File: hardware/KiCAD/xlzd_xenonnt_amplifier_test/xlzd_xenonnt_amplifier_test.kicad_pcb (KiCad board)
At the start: 4 copper layers, 34 x 60 mm, 25 parts, among them J1 Conn_Coaxial, J2 Conn_Coaxial, J3 Conn_Coaxial, J4 Screw_Terminal_01x03, U1 OPA847xDBV, U3 OPA692xDBV

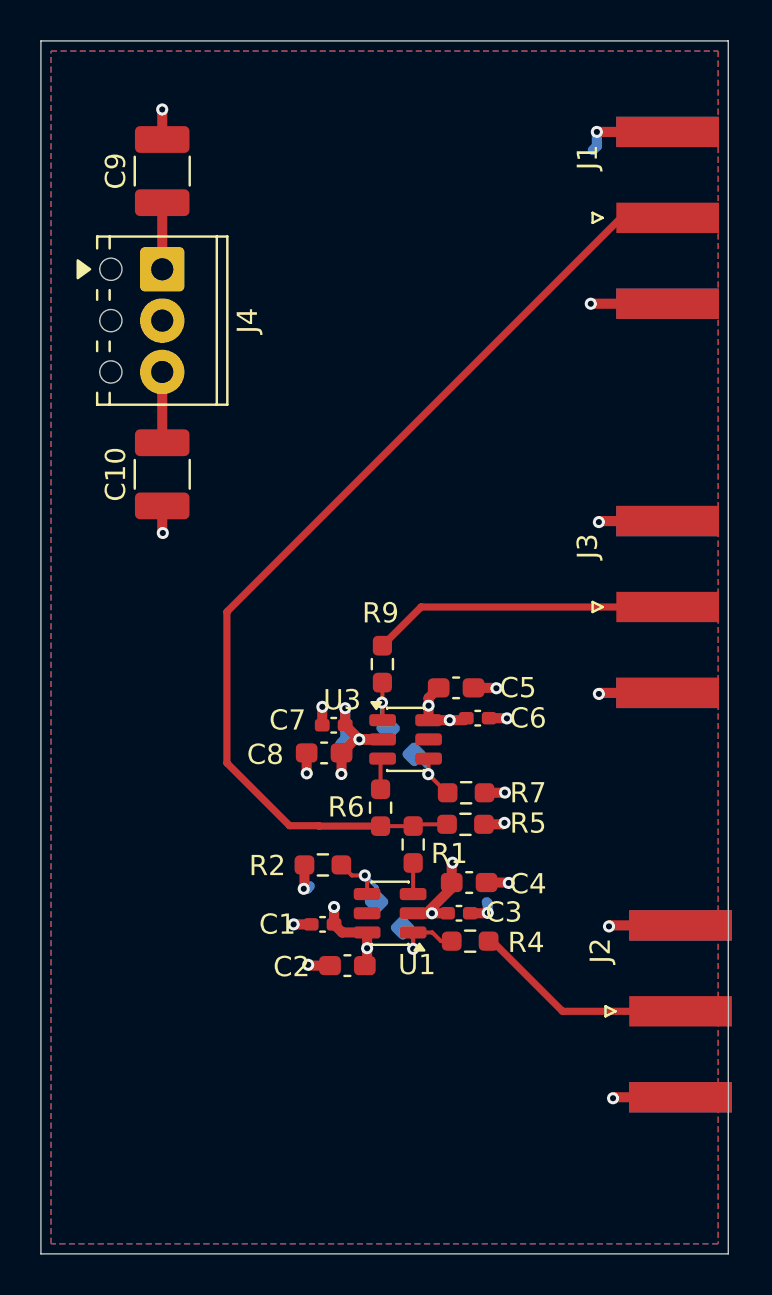
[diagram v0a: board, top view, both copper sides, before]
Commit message: Generated manufacturing artwork
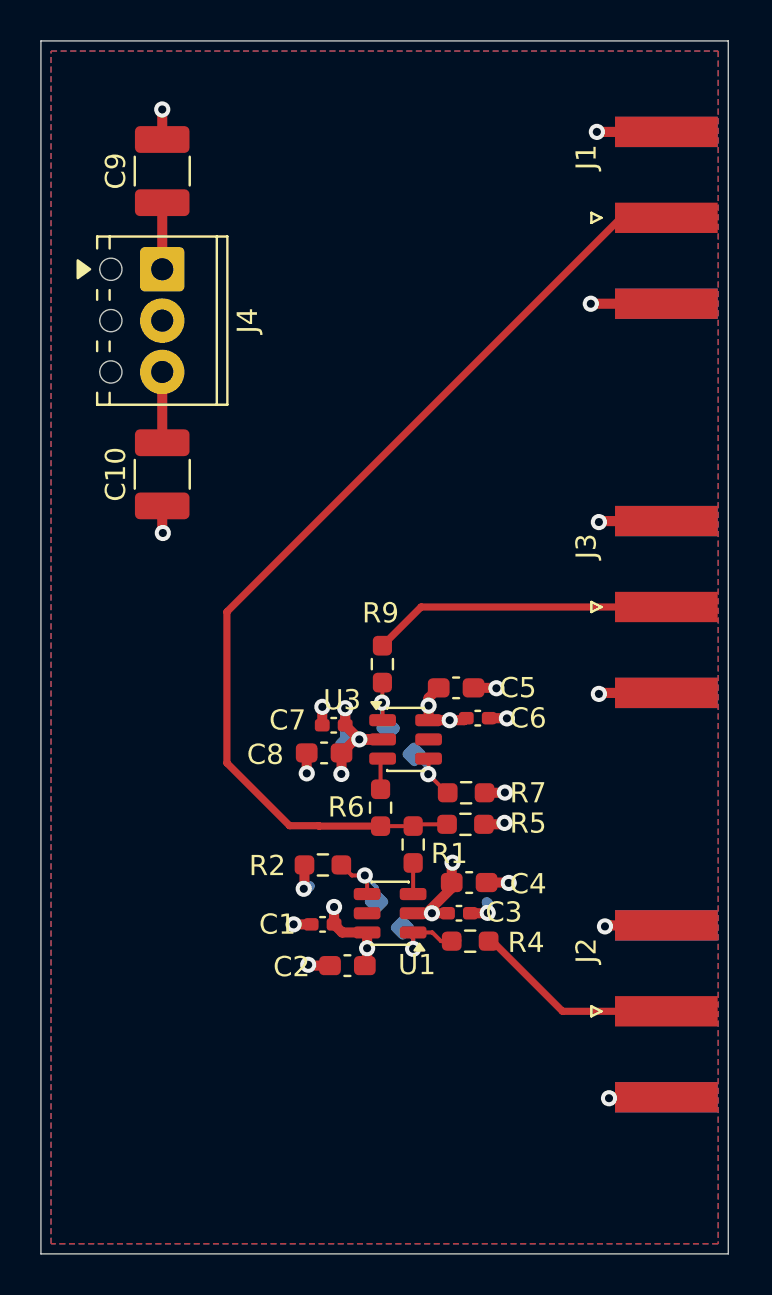
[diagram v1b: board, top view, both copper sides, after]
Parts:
- moved J2 0.70 mm to (75.9, 110.0)
- moved J1 0.06 mm to (75.9, 70.8)
- moved J3 0.06 mm to (75.9, 90.0)
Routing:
- net GND: track 36.9 -> 35.9 mm
- net /vout_high_g: track 10.9 -> 10.3 mm
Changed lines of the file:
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@@
 		(capping no)
 		(filling no)
-		(zone_defaults)
 		(pcbplotparams
 			(layerselection 0x00000000_00000000_55555555_5755f5ff)
@@
 	(footprint "Connector_Coaxial:SMA_Amphenol_132289_EdgeMount"
 		(layer "F.Cu")
-		(at 76 70.75)
+		(at 75.9375 70.75)
 		(descr "https://www.amphenolrf.com/library/download/link/link_id/595984/parent/132289/")
 		(tags "SMA")
@@
 	(footprint "Connector_Coaxial:SMA_Amphenol_132289_EdgeMount"
 		(layer "F.Cu")
-		(at 76 90)
+		(at 75.9375 90)
 		(descr "https://www.amphenolrf.com/library/download/link/link_id/595984/parent/132289/")
 		(tags "SMA")
@@
 	(footprint "Connector_Coaxial:SMA_Amphenol_132289_EdgeMount"
 		(layer "F.Cu")
-		(at 76.6375 110)
+		(at 75.9375 110)
 		(descr "https://www.amphenolrf.com/library/download/link/link_id/595984/parent/132289/")
 		(tags "SMA")
@@
 	(via
 		(at 68.05 95.51)
-		(size 0.6)
-		(drill 0.3)
+		(size 0.8)
+		(drill 0.4)
 		(layers "F.Cu" "B.Cu")
 		(net "GND")
@@
 	(via
 		(at 51 65.39)
-		(size 0.6)
-		(drill 0.3)
+		(size 0.8)
+		(drill 0.4)
 		(layers "F.Cu" "B.Cu")
 		(net "GND")
 	)
 	(via
-		(at 73.1 105.8)
-		(size 0.6)
-		(drill 0.3)
+		(at 72.9 105.8)
+		(size 0.8)
+		(drill 0.4)
 		(layers "F.Cu" "B.Cu")
 		(net "GND")
@@
 	(via
 		(at 58 103.94)
-		(size 0.6)
-		(drill 0.3)
+		(size 0.8)
+		(drill 0.4)
 		(layers "F.Cu" "B.Cu")
 		(net "GND")
@@
 	(via
 		(at 72.6 85.8)
-		(size 0.6)
-		(drill 0.3)
+		(size 0.8)
+		(drill 0.4)
 		(layers "F.Cu" "B.Cu")
 		(net "GND")
@@
 	(via
 		(at 72.2 75)
-		(size 0.6)
-		(drill 0.3)
+		(size 0.8)
+		(drill 0.4)
 		(layers "F.Cu" "B.Cu")
 		(net "GND")
@@
 	(via
 		(at 58.15 98.23)
-		(size 0.6)
-		(drill 0.3)
+		(size 0.8)
+		(drill 0.4)
 		(layers "F.Cu" "B.Cu")
 		(net "GND")
@@
 	(via
 		(at 67.93 100.68)
-		(size 0.6)
-		(drill 0.3)
+		(size 0.8)
+		(drill 0.4)
 		(layers "F.Cu" "B.Cu")
 		(net "GND")
@@
 	(via
 		(at 51.03 86.34)
-		(size 0.6)
-		(drill 0.3)
+		(size 0.8)
+		(drill 0.4)
 		(layers "F.Cu" "B.Cu")
 		(net "GND")
 	)
 	(via
-		(at 73.3 114.3)
-		(size 0.6)
-		(drill 0.3)
+		(at 73.1 114.3)
+		(size 0.8)
+		(drill 0.4)
 		(layers "F.Cu" "B.Cu")
 		(net "GND")
@@
 	(via
 		(at 58.92 94.94)
-		(size 0.6)
-		(drill 0.3)
+		(size 0.8)
+		(drill 0.4)
 		(layers "F.Cu" "B.Cu")
 		(net "GND")
@@
 	(via
 		(at 72.5 66.5)
-		(size 0.6)
-		(drill 0.3)
+		(size 0.8)
+		(drill 0.4)
 		(layers "F.Cu" "B.Cu")
 		(net "GND")
@@
 	(via
 		(at 67.53 94.02)
-		(size 0.6)
-		(drill 0.3)
+		(size 0.8)
+		(drill 0.4)
 		(layers "F.Cu" "B.Cu")
 		(net "GND")
@@
 	(via
 		(at 67.95 99.18)
-		(size 0.6)
-		(drill 0.3)
+		(size 0.8)
+		(drill 0.4)
 		(layers "F.Cu" "B.Cu")
 		(net "GND")
@@
 	(via
 		(at 58.22 107.7)
-		(size 0.6)
-		(drill 0.3)
+		(size 0.8)
+		(drill 0.4)
 		(layers "F.Cu" "B.Cu")
 		(net "GND")
@@
 	(via
 		(at 67.1 105.13)
-		(size 0.6)
-		(drill 0.3)
+		(size 0.8)
+		(drill 0.4)
 		(layers "F.Cu" "B.Cu")
 		(net "GND")
@@
 	(via
 		(at 68.14 103.65)
-		(size 0.6)
-		(drill 0.3)
+		(size 0.8)
+		(drill 0.4)
 		(layers "F.Cu" "B.Cu")
 		(net "GND")
@@
 	(via
 		(at 72.6 94.3)
-		(size 0.6)
-		(drill 0.3)
+		(size 0.8)
+		(drill 0.4)
 		(layers "F.Cu" "B.Cu")
 		(net "GND")
@@
 	(via
 		(at 57.5 105.7)
-		(size 0.6)
-		(drill 0.3)
+		(size 0.8)
+		(drill 0.4)
 		(layers "F.Cu" "B.Cu")
 		(net "GND")
@@
 	)
 	(segment
-		(start 72.5 66.5)
-		(end 72.5 67.2)
-		(width 0.5)
-		(layer "B.Cu")
-		(net "GND")
-	)
-	(segment
 		(start 58.92 94.94)
 		(end 58.94 94.92)
@@
 	)
 	(segment
-		(start 72.5 67.2)
-		(end 72.3 67.4)
-		(width 0.5)
-		(layer "B.Cu")
-		(net "GND")
-	)
-	(segment
 		(start 67.1 104.65)
 		(end 67.05 104.6)
@@
 	(via
 		(at 60.750001 96.550001)
-		(size 0.6)
-		(drill 0.3)
+		(size 0.8)
+		(drill 0.4)
 		(layers "F.Cu" "B.Cu")
 		(net "VEE")
@@
 	(via
 		(at 65.36 102.65)
-		(size 0.6)
-		(drill 0.3)
+		(size 0.8)
+		(drill 0.4)
 		(layers "F.Cu" "B.Cu")
 		(net "VEE")
@@
 	(via
 		(at 64.34 105.15)
-		(size 0.6)
-		(drill 0.3)
+		(size 0.8)
+		(drill 0.4)
 		(layers "F.Cu" "B.Cu")
 		(net "VEE")
@@
 	(via
 		(at 60.05 95.01)
-		(size 0.6)
-		(drill 0.3)
+		(size 0.8)
+		(drill 0.4)
 		(layers "F.Cu" "B.Cu")
 		(net "VEE")
@@
 	(via
 		(at 59.86 98.26)
-		(size 0.6)
-		(drill 0.3)
+		(size 0.8)
+		(drill 0.4)
 		(layers "F.Cu" "B.Cu")
 		(net "VEE")
@@
 	(via
 		(at 64.16 98.27)
-		(size 0.6)
-		(drill 0.3)
+		(size 0.8)
+		(drill 0.4)
 		(layers "F.Cu" "B.Cu")
 		(net "Net-(U3--)")
@@
 	(via
 		(at 63.41 106.91)
-		(size 0.6)
-		(drill 0.3)
+		(size 0.8)
+		(drill 0.4)
 		(layers "F.Cu" "B.Cu")
 		(net "Net-(R3-Pad2)")
@@
 	(via
 		(at 61.02 103.28)
-		(size 0.6)
-		(drill 0.3)
+		(size 0.8)
+		(drill 0.4)
 		(layers "F.Cu" "B.Cu")
 		(net "Net-(U1--)")
@@
 	(via
 		(at 61.135 106.88)
-		(size 0.6)
-		(drill 0.3)
+		(size 0.8)
+		(drill 0.4)
 		(layers "F.Cu" "B.Cu")
 		(net "VCC")
@@
 	(via
 		(at 59.5 104.84)
-		(size 0.6)
-		(drill 0.3)
+		(size 0.8)
+		(drill 0.4)
 		(layers "F.Cu" "B.Cu")
 		(net "VCC")
@@
 	(via
 		(at 64.175 94.88)
-		(size 0.6)
-		(drill 0.3)
+		(size 0.8)
+		(drill 0.4)
 		(layers "F.Cu" "B.Cu")
 		(net "VCC")
@@
 	(via
 		(at 65.22 95.600002)
-		(size 0.6)
-		(drill 0.3)
+		(size 0.8)
+		(drill 0.4)
 		(layers "F.Cu" "B.Cu")
 		(net "VCC")
 	)
 	(segment
-		(start 67.145 106.53)
-		(end 67.33 106.53)
+		(start 70.8 110)
+		(end 76 110)
 		(width 0.355)
 		(layer "F.Cu")
@@
 	)
 	(segment
-		(start 67.33 106.53)
-		(end 70.8 110)
+		(start 67.145 106.53)
+		(end 67.33 106.53)
 		(width 0.355)
 		(layer "F.Cu")
@@
 	)
 	(segment
-		(start 70.8 110)
-		(end 76.6375 110)
+		(start 67.33 106.53)
+		(end 70.8 110)
 		(width 0.355)
 		(layer "F.Cu")
@@
 	(via
 		(at 61.87 94.73)
-		(size 0.6)
-		(drill 0.3)
+		(size 0.8)
+		(drill 0.4)
 		(layers "F.Cu" "B.Cu")
 		(net "Net-(R8-Pad2)")

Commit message: Tidied up silkscreen. Added fabrication drawings to Gerber job
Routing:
- net GND: track 35.9 -> 35.2 mm
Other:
- board text added: "+5V GND -5V"
- board text added: "Input"
- board text added: "Out High Gain"
- board text added: "Out Low Gain"
- board text added: "UoB HEP pc078 XLZD OD amp"
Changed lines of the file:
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@@
 		(filling no)
 		(pcbplotparams
-			(layerselection 0x00000000_00000000_55555555_5755f5ff)
+			(layerselection 0x00000000_00000000_5555555f_5757f5ff)
 			(plot_on_all_layers_selection 0x00000000_00000000_00000000_00000000)
 			(disableapertmacros no)
@@
 			(dashed_line_gap_ratio 3)
 			(svgprecision 4)
-			(plotframeref no)
+			(plotframeref yes)
 			(mode 1)
 			(useauxorigin no)
@@
 			(sketchdnponfab yes)
 			(crossoutdnponfab yes)
-			(subtractmaskfromsilk no)
+			(subtractmaskfromsilk yes)
 			(outputformat 1)
 			(mirror no)
-			(drillshape 1)
+			(drillshape 0)
 			(scaleselection 1)
-			(outputdirectory "")
+			(outputdirectory "Manufacturing")
 		)
 	)
@@
 		(tags "SMA")
 		(property "Reference" "J1"
-			(at -3.96 -3 90)
+			(at -6.1375 -4.15 180)
 			(layer "F.SilkS")
 			(effects
@@
 		)
 		(property "Value" "27R"
-			(at 0 1.43 90)
+			(at 0 -1.6 90)
 			(layer "F.Fab")
 			(effects
@@
 		)
 		(property "Value" "100n"
-			(at 0 1.43 0)
+			(at 3.607499 0.22 0)
 			(layer "F.Fab")
 			(effects
@@
 		)
 		(property "Value" "51"
-			(at 0 1.43 0)
+			(at 3 0.25 0)
 			(layer "F.Fab")
 			(effects
@@
 		)
 		(property "Value" "OPEN"
-			(at 0 1.43 0)
+			(at 4.0675 0.11 0)
 			(layer "F.Fab")
 			(effects
@@
 		)
 		(property "Value" "OPA847xDBV"
-			(at 0 2.4 0)
+			(at -4.6275 -2.949999 0)
 			(layer "F.Fab")
 			(effects
@@
 		)
 		(property "Value" "51R"
-			(at 0 1.43 0)
+			(at 3.3675 0.17 0)
 			(layer "F.Fab")
 			(effects
@@
 		)
 		(fp_text user "${REFERENCE}"
-			(at 0 0 0)
+			(at 3.7675 -1.36 0)
 			(layer "F.Fab")
 			(effects
@@
 		)
 		(property "Value" "OPA692xDBV"
-			(at 0 2.4 0)
+			(at -7.1375 -2.750001 0)
 			(layer "F.Fab")
 			(effects
@@
 		)
 		(property "Value" "100n"
-			(at 0 1.43 0)
+			(at 3.6625 0 0)
 			(layer "F.Fab")
 			(effects
@@
 		)
 		(property "Value" "1n"
-			(at 0 1.16 0)
+			(at 2.3925 0 0)
 			(layer "F.Fab")
 			(effects
@@
 		)
 		(property "Value" "27R"
-			(at 0 1.43 90)
+			(at -3.05 -0.0875 90)
 			(layer "F.Fab")
 			(effects
@@
 		(tags "SMA")
 		(property "Reference" "J3"
-			(at -3.96 -3 90)
+			(at -0.0375 -7.1 180)
 			(layer "F.SilkS")
 			(effects
@@
 		(tags "SMA")
 		(property "Reference" "J2"
-			(at -3.96 -3 90)
+			(at -0.4375 -7 180)
 			(layer "F.SilkS")
 			(effects
@@
 		)
 		(property "Value" "1n"
-			(at 0 1.16 0)
+			(at 3.1225 0.05 0)
 			(layer "F.Fab")
 			(effects
@@
 		)
 		(fp_text user "${REFERENCE}"
-			(at 0 0 0)
+			(at 3.7675 -1.36 0)
 			(layer "F.Fab")
 			(effects
@@
 		)
 		(property "Value" "100n"
-			(at 0 1.43 0)
+			(at 3.7675 0.07 0)
 			(layer "F.Fab")
 			(effects
@@
 		)
 		(property "Value" "27R"
-			(at 0 1.43 0)
+			(at 3.2475 -0.04 0)
 			(layer "F.Fab")
 			(effects
@@
 		)
 		(property "Value" "1n"
-			(at 0 1.16 0)
+			(at 2.3825 0.25 0)
 			(layer "F.Fab")
 			(effects
@@
 		)
 		(property "Value" "1n"
-			(at 0 1.16 0)
+			(at 2.6325 0.2 0)
 			(layer "F.Fab")
 			(effects
@@
 		)
 		(property "Value" "100n"
-			(at 0 1.43 0)
+			(at 3.46 0.04 0)
 			(layer "F.Fab")
 			(effects
@@
 		(tags "THT Terminal Block Phoenix MPT-0,5-3-2.54 pitch 2.54mm size 8.08x6.2mm drill 1.1mm pad 2.2mm")
 		(property "Reference" "J4"
-			(at 2.54 -4.22 90)
+			(at 8.304999 -3.4 180)
 			(layer "F.SilkS")
 			(effects
@@
 		(layer "Edge.Cuts")
 	)
+	(gr_text "Input"
+		(at 65.4 71.5 0)
+		(layer "F.SilkS")
+		(effects
+			(font
+				(size 1.5 1.5)
+				(thickness 0.3)
+				(bold yes)
+			)
+			(justify left bottom)
+		)
+	)
+	(gr_text "Out\nLow\nGain"
+		(at 66.5 90.4 0)
+		(layer "F.SilkS")
+		(effects
+			(font
+				(size 1.5 1.5)
+				(thickness 0.3)
+				(bold yes)
+			)
+			(justify left bottom)
+		)
+	)
+	(gr_text "Out\nHigh\nGain"
+		(at 66.8 115.5 0)
+		(layer "F.SilkS")
+		(effects
+			(font
+				(size 1.5 1.5)
+				(thickness 0.3)
+				(bold yes)
+			)
+			(justify left bottom)
+		)
+	)
+	(gr_text "UoB HEP \npc078\nXLZD OD amp"
+		(at 46.6 120 0)
+		(layer "F.SilkS")
+		(effects
+			(font
+				(size 2 2)
+				(thickness 0.25)
+			)
+			(justify left bottom)
+		)
+	)
+	(gr_text "+5V\nGND\n-5V"
+		(at 54.9 80.2 0)
+		(layer "F.SilkS")
+		(effects
+			(font
+				(size 2 2)
+				(thickness 0.4)
+				(bold yes)
+			)
+			(justify left bottom)
+		)
+	)
 	(dimension
 		(type orthogonal)
@@
 	)
 	(segment
-		(start 58.17 103.94)
-		(end 58.3 103.81)
-		(width 0.5)
-		(layer "B.Cu")
-		(net "GND")
-	)
-	(segment
 		(start 58 103.94)
 		(end 58.17 103.94)
@@
 		(width 0.5)
 		(layer "B.Cu")
-		(net "GND")
-	)
-	(segment
-		(start 67.1 105.13)
-		(end 67.1 104.65)
-		(width 0.5)
-		(layer "B.Cu")
-		(net "GND")
-	)
-	(segment
-		(start 67.1 104.65)
-		(end 67.05 104.6)
-		(width 0.5)
-		(layer "B.Cu")

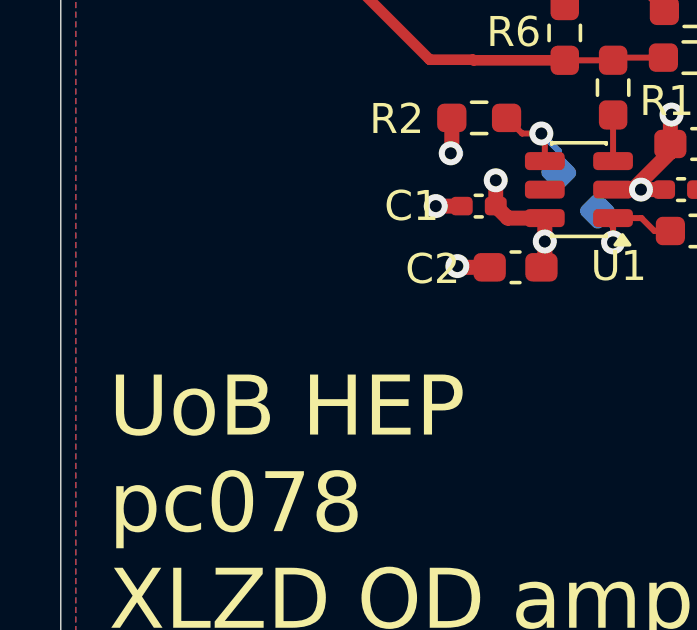
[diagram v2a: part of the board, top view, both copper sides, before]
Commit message: Added voids to planes underneath inverting input to op-amps. Regenerated artwork. Created Zip archive
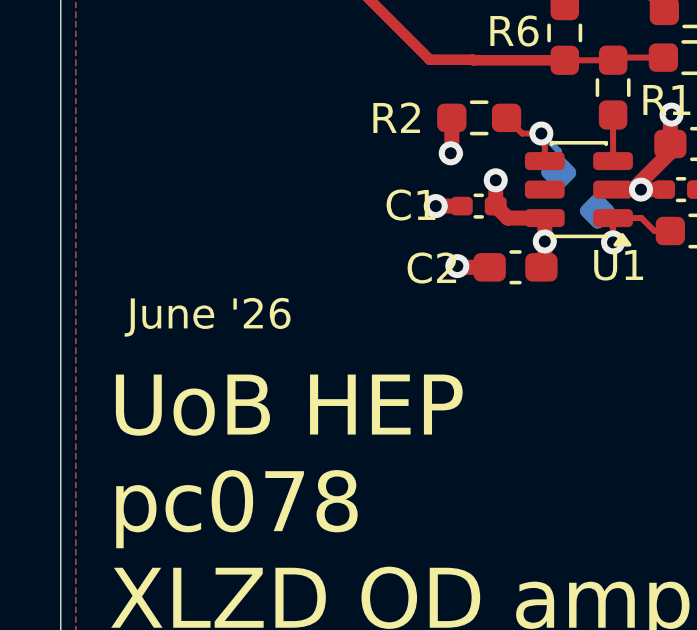
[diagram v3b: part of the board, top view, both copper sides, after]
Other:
- board text added: "June '26"
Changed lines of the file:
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@@
 		(layer "Edge.Cuts")
+	)
+	(gr_text "June '26"
+		(at 47.2 109.9 0)
+		(layer "F.SilkS")
+		(effects
+			(font
+				(size 1 1)
+				(thickness 0.15)
+			)
+			(justify left bottom)
+		)
 	)
 	(gr_text "Input"
@@
 			)
 		)
+	)
+	(zone
+		(layers "B.Cu" "In1.Cu" "In2.Cu" "User.4")
+		(hatch edge 0.5)
+		(connect_pads
+			(clearance 0)
+		)
+		(min_thickness 0.25)
+		(keepout
+			(tracks allowed)
+			(vias allowed)
+			(pads allowed)
+			(copperpour not_allowed)
+			(footprints allowed)
+		)
+		(placement
+			(enabled no)
+			(sheetname "/")
+		)
+		(fill
+			(thermal_gap 0.5)
+			(thermal_bridge_width 0.5)
+			(island_removal_mode 0)
+		)
+		(polygon
+			(pts
+				(xy 65 97) (xy 63.3 97) (xy 63.3 98.4) (xy 64.4 99.7) (xy 65.9 99.7) (xy 65.9 98.5)
+			)
+		)
+	)
+	(zone
+		(layers "B.Cu" "In1.Cu" "In2.Cu" "User.4")
+		(hatch edge 0.5)
+		(connect_pads
+			(clearance 0)
+		)
+		(min_thickness 0.25)
+		(keepout
+			(tracks allowed)
+			(vias allowed)
+			(pads allowed)
+			(copperpour not_allowed)
+			(footprints allowed)
+		)
+		(placement
+			(enabled no)
+			(sheetname "/")
+		)
+		(fill
+			(thermal_gap 0.5)
+			(thermal_bridge_width 0.5)
+			(island_removal_mode 0)
+		)
+		(polygon
+			(pts
+				(xy 61.9 104.7) (xy 60.3 104.7) (xy 60.3 103.9) (xy 59.2 103.3) (xy 59.2 102.1) (xy 60.6 102.1)
+				(xy 61.9 103)
+			)
+		)
